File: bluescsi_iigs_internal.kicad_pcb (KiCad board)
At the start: 2 copper layers, 56.6 x 53.3 mm, 16 parts, among them J1 Conn_02x13_Odd_Even, J2 Conn_02x13_Odd_Even, J3 Micro_SD_Card, SW1 SW_SPDT, U1 YAAJ_BluePill, U2 UCC5606, U3 UCC5606

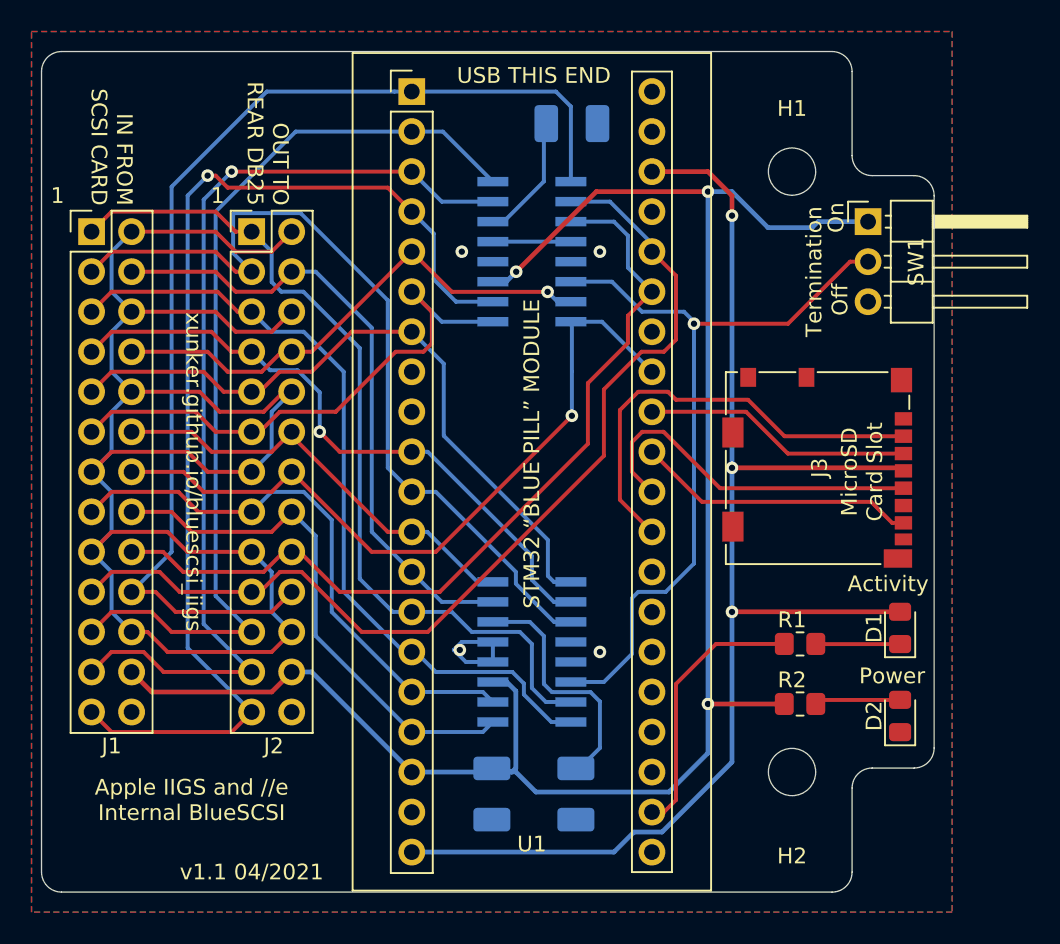
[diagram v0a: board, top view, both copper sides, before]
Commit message: Change switch to smd
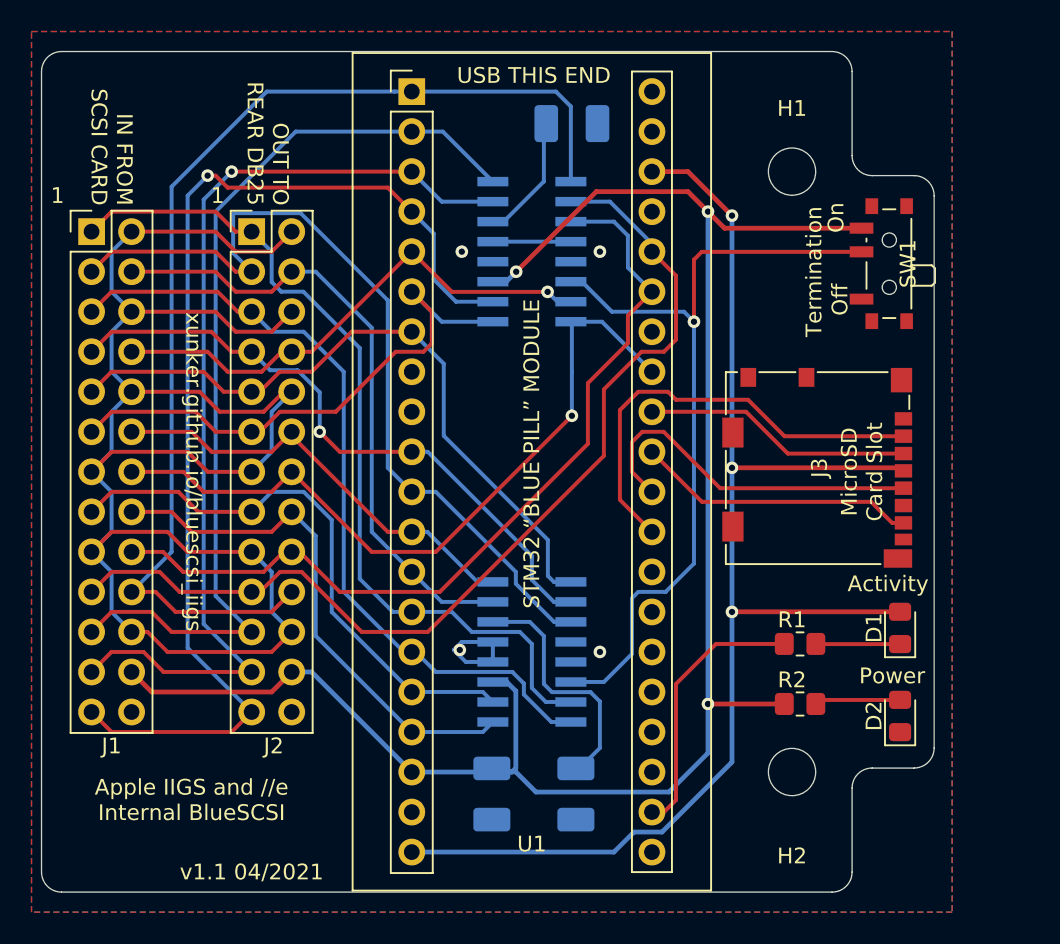
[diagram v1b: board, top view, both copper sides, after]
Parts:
- SW1: footprint Connector_PinHeader_2.54mm:PinHeader_1x03_P2.54mm_Horizontal -> Button_Switch_SMD:SW_SPDT_PCM12
- moved SW1 2.85 mm to (182.4, 61.7), turned to 90 degrees
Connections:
- SW1 pad 1: +5V -> GND
- SW1 pad 3: GND -> +5V
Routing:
- net /TERM_DISC: track 49.9 -> 52.0 mm
- net +5V: track 118.5 -> 116.7 mm
- net +3V3: track 86.1 -> 85.4 mm
